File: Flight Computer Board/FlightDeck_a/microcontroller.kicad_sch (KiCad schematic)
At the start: 1 part, among them U1 STM32F405RGTx

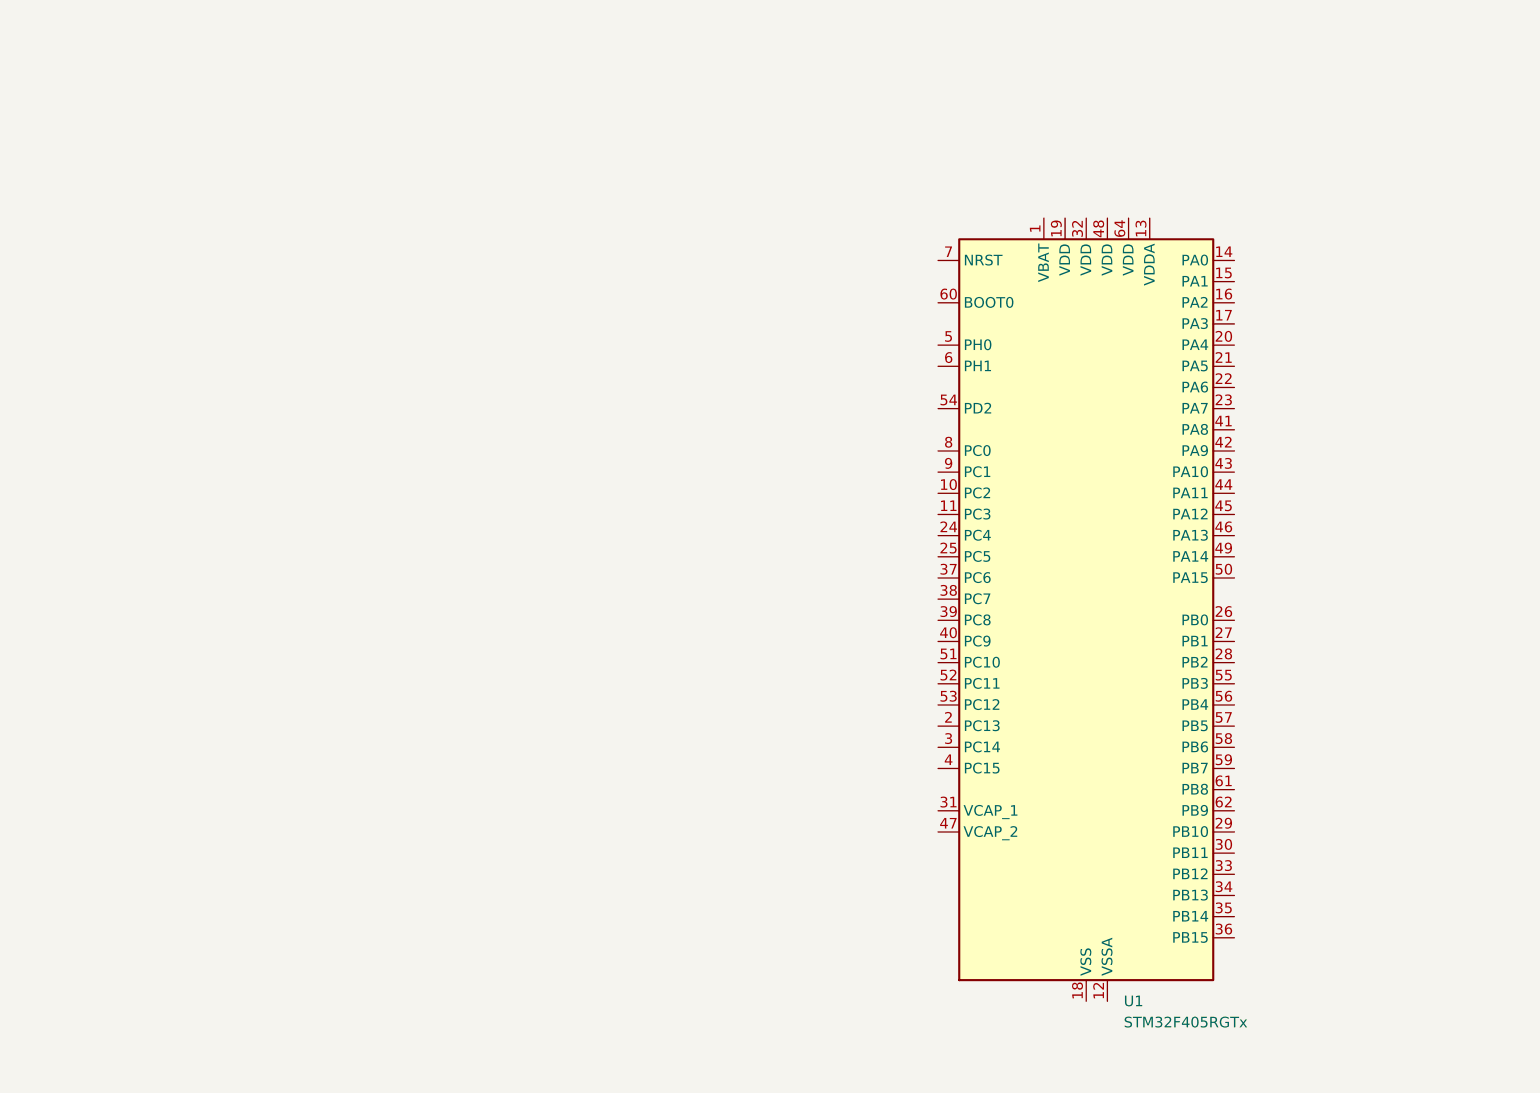
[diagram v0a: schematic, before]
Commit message: added power and ground
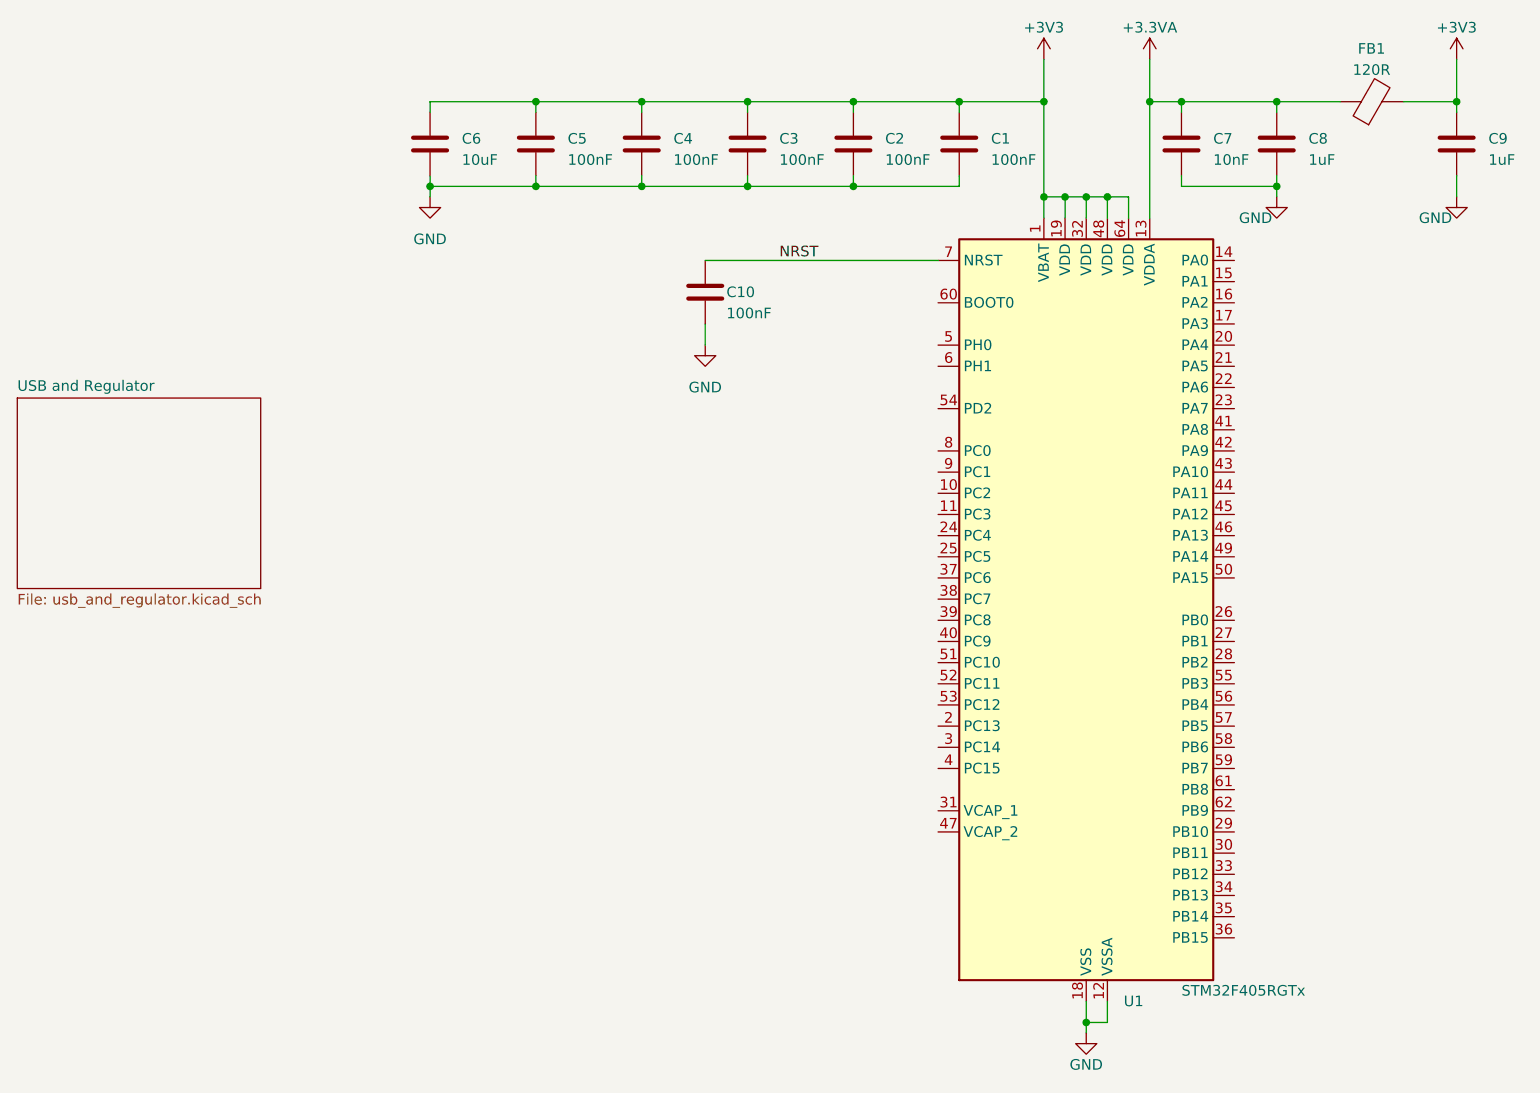
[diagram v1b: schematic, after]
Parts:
- added C1, C10, C2, C3, C4, C5: 100nF, symbol Device:C
- added C6: 10uF, symbol Device:C
- added C7: 10nF, symbol Device:C
- added C8, C9: 1uF, symbol Device:C
- added FB1: 120R, symbol Device:FerriteBead
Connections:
- net +3V3: now reaches U1.1 (VBAT)
- net +3V3: now also U1.19 (VDD), U1.32 (VDD), U1.48 (VDD), U1.64 (VDD), C1.1, C2.1, C3.1, C4.1, C5.1, C6.1, C9.1, FB1.2
- net GND: now reaches U1.12 (VSSA)
- net GND: now also U1.18 (VSS), U1.63 (VSS), C1.2, C10.2, C2.2, C3.2, C4.2, C5.2, C6.2, C7.2, C8.2, C9.2
- net +3.3VA: now reaches U1.13 (VDDA)
- net +3.3VA: now also C7.1, C8.1, FB1.1
- net NRST: now reaches U1.7 (NRST)
- net NRST: now also C10.1
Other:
- added sheet USB and Regulator (usb_and_regulator.kicad_sch)
